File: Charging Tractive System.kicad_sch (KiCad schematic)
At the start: 2 parts, among them SW1 SW_Push_Open

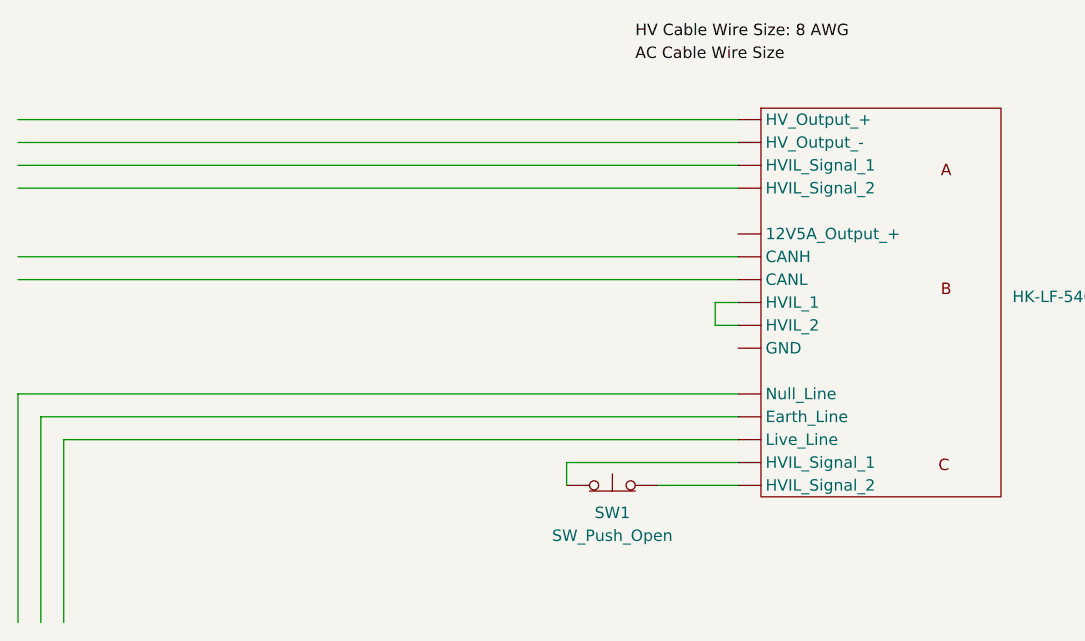
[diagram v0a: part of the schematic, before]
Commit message: finish wiring charger to bms
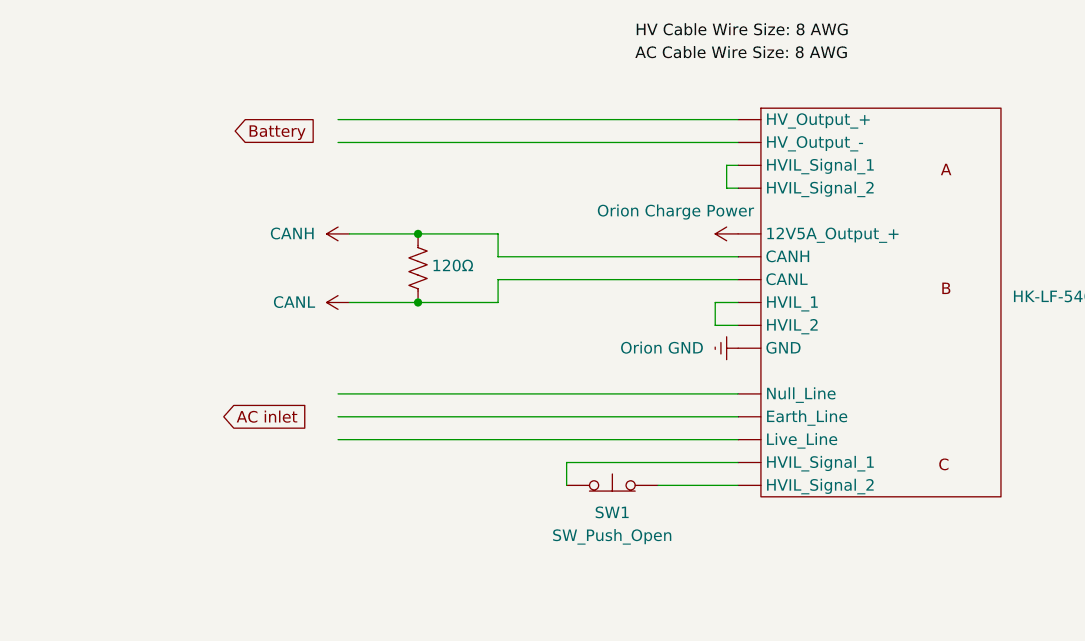
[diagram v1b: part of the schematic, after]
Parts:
- added 120Ω: R_US, symbol Device:R_US
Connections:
- net Orion GND: now reaches HK-LF-540-12. (Null_Line)
- new net CANH: 120Ω.1, HK-LF-540-12. (Null_Line)
- new net CANL: 120Ω.2, HK-LF-540-12. (Null_Line)
- new net Orion Charge Power: HK-LF-540-12. (Null_Line)

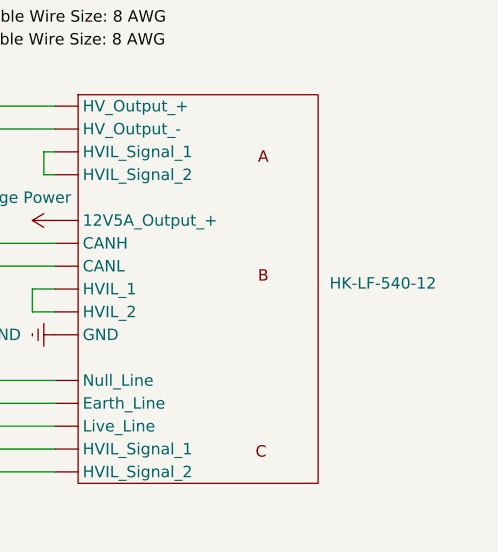
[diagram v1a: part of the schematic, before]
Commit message: change out charger
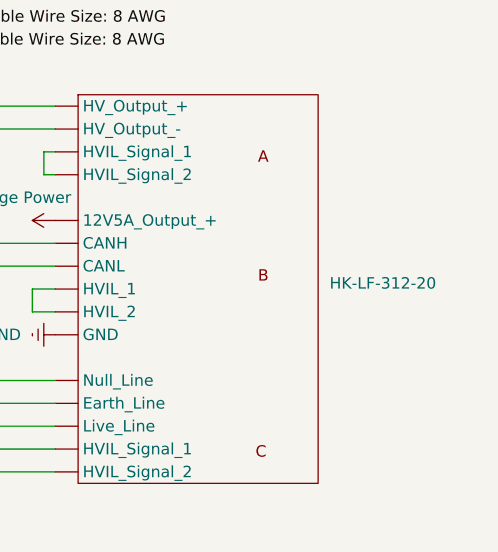
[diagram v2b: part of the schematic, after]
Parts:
- renumbered HK-LF-540-12 to HK-LF-312-20
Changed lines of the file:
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@@
 		(dnp no)
 		(fields_autoplaced yes)
-		(property "Reference" "HK-LF-540-12"
+		(property "Reference" "HK-LF-312-20"
 			(at 186.69 122.5549 0)
 			(effects
@@
 			(project ""
 				(path "/3ff09eae-d3c8-46ca-b652-20f4f82d766c"
-					(reference "HK-LF-540-12")
+					(reference "HK-LF-312-20")
 					(unit 1)
 				)

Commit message: update with TSMP
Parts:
- added 15kΩ: TSMP1, symbol Device:R_US
- added 15kΩ: TSMP2, symbol Device:R_US
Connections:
- new net: 15kΩ.1, 15kΩ.1, HK-LF-312-20. (Null_Line)
- new net: 15kΩ.2, 15kΩ.2, HK-LF-312-20. (Null_Line)

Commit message: add IMS
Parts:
- added iso175: ~, symbol Charging Tractive System:iso175
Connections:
- net CANH: now also iso175. (V-)
- net CANL: now also iso175. (V-)
- net Orion GND: now also iso175. (V-)
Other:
- moved on the sheet: 120Ω, 15kΩ, HK-LF-312-20, SW1

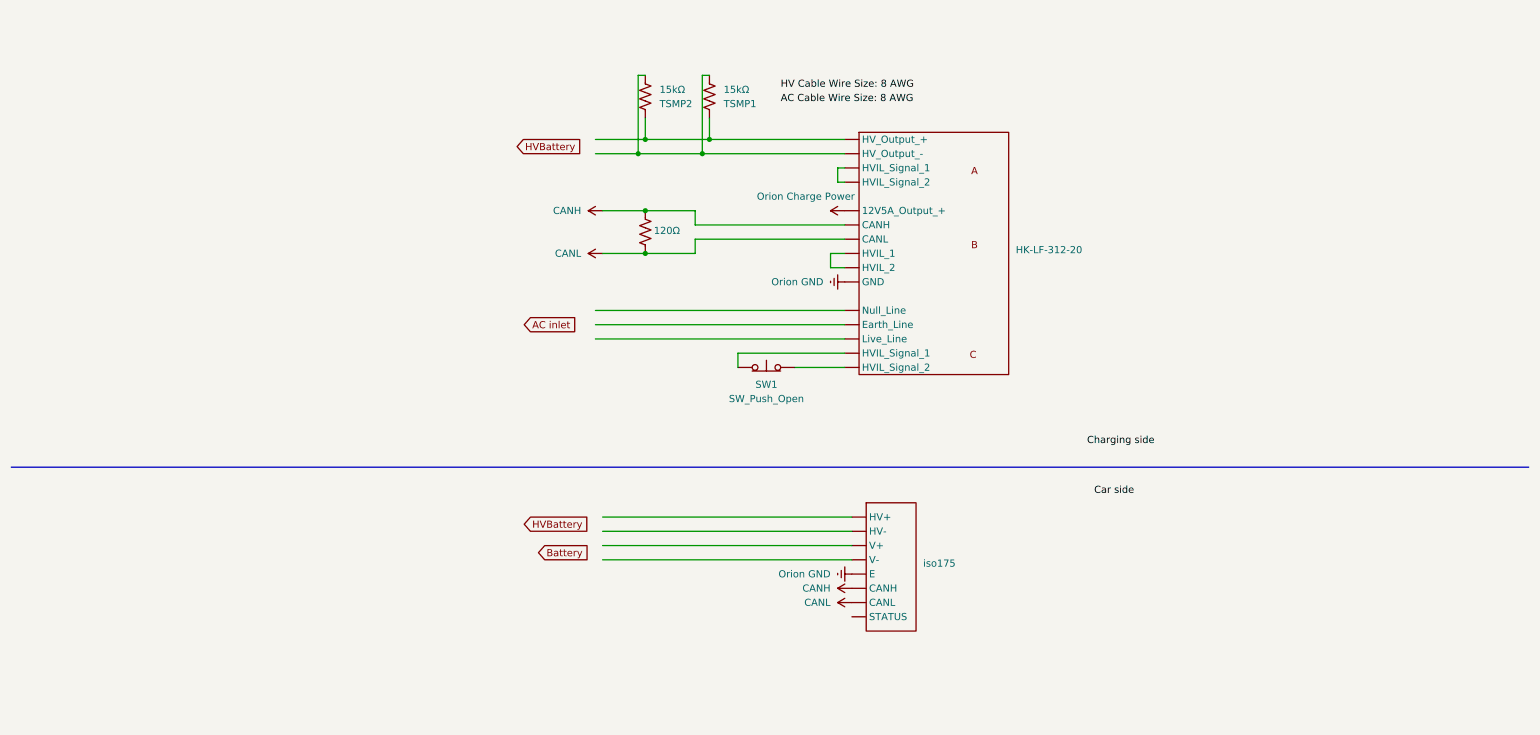
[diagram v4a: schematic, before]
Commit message: update with BMS
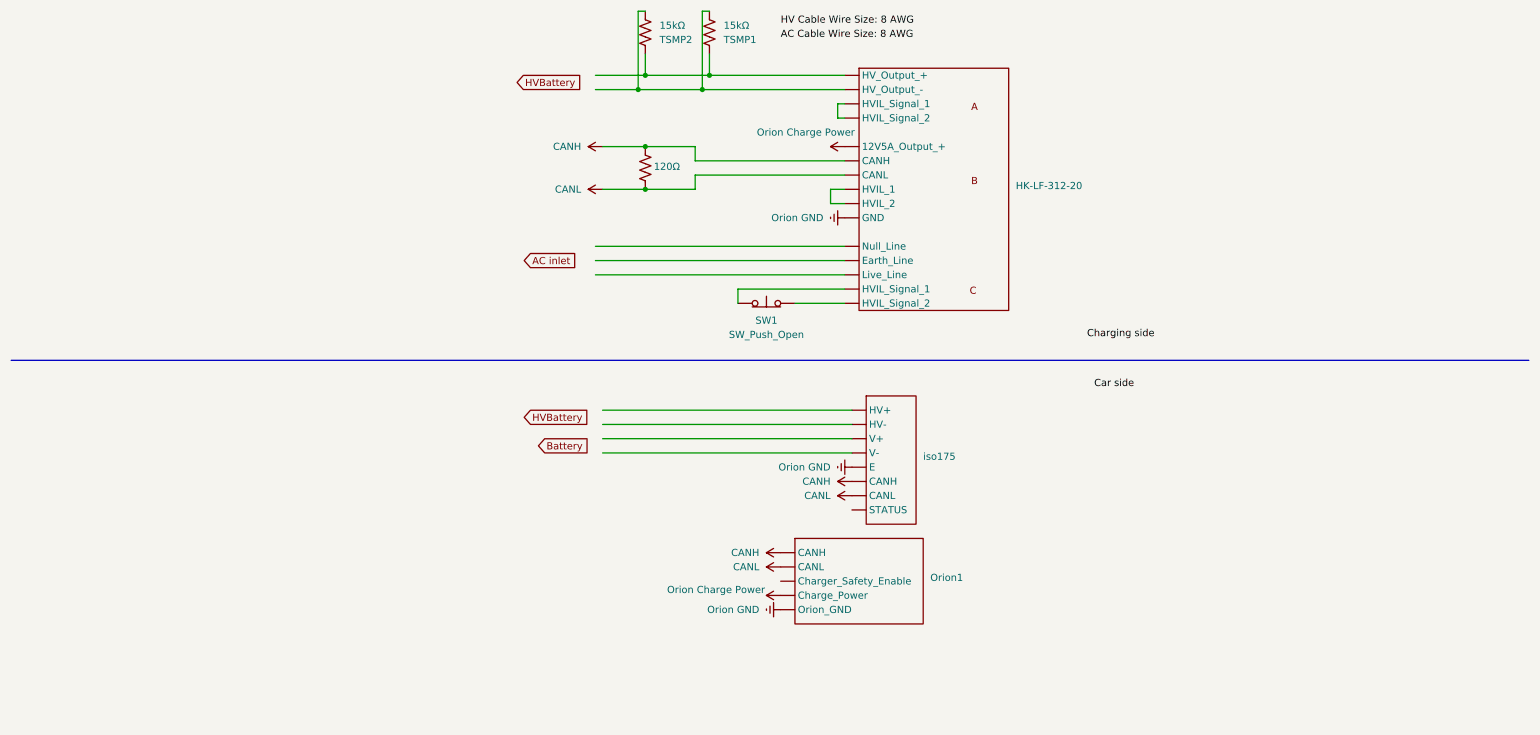
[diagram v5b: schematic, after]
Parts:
- added Orion1: ~, symbol Charging Tractive System:Orion_2
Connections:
- net CANH: now also Orion1. (Orion_GND)
- net CANL: now also Orion1. (Orion_GND)
- net Orion Charge Power: now also Orion1. (Orion_GND)
- net Orion GND: now also Orion1. (Orion_GND)
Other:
- moved on the sheet: 120Ω, 15kΩ, HK-LF-312-20, SW1, iso175

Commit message: update schem
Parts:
- renumbered Orion1 to Orion2
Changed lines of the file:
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@@
 		(dnp no)
 		(fields_autoplaced yes)
-		(property "Reference" "Orion1"
+		(property "Reference" "Orion2"
 			(at 177.8 132.7149 0)
 			(effects
@@
 			(project ""
 				(path "/3ff09eae-d3c8-46ca-b652-20f4f82d766c"
-					(reference "Orion1")
+					(reference "Orion2")
 					(unit 1)
 				)
